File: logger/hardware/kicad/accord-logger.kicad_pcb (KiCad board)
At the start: 2 copper layers, 120 x 80 mm, 72 parts, among them J1 Board connector 14-way, J3 Spare GP13 / switched power, J4 Reset RUN-GND, J5 SD breakout 6-way, Q5 IPD50P04P4L-11, Q6 2N3904, Q7 2N3904, U1 RaspberryPi_Pico_W, U15 MAX3485, U16 DS3231SN, U6 LM2678T-5.0

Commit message: layout: thermal relief fixed at J1 pin 2 and Q6 pin 1
Ground tracks added at both pads. Refilled scratch DRC: no errors beyond
the Pico footprint's own paste items; parity 0; unconnected only Q5's
middle lead; the SUPPLY_ADC via and VSS_IN stub are intentional.

Claude-Session-ID: 42dd0e33-28b5-4936-847e-9c2e1d2488fa
Co-Authored-By: Claude Opus 5.5 <noreply@anthropic.com>
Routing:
- net /PGND: track 40.8 -> 51.8 mm, vias 18 -> 22
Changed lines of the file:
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@@
 		(net 3)
 	)
+	(segment
+		(start 183.515 92.71)
+		(end 184.025 92.2)
+		(width 0.3)
+		(layer "F.Cu")
+		(net 4)
+	)
+	(segment
+		(start 184.025 92.2)
+		(end 185.7325 92.2)
+		(width 0.3)
+		(layer "F.Cu")
+		(net 4)
+	)
+	(segment
+		(start 152.4 101.6)
+		(end 152.4 100.965)
+		(width 0.3)
+		(layer "F.Cu")
+		(net 4)
+	)
+	(segment
+		(start 187.96 92.71)
+		(end 187.45 92.2)
+		(width 0.3)
+		(layer "F.Cu")
+		(net 4)
+	)
+	(segment
+		(start 187.45 92.2)
+		(end 185.7325 92.2)
+		(width 0.3)
+		(layer "F.Cu")
+		(net 4)
+	)
+	(segment
+		(start 152.4 100.965)
+		(end 153.67 99.695)
+		(width 0.3)
+		(layer "F.Cu")
+		(net 4)
+	)
 	(via
 		(at 151.765 79.375)
@@
 	)
 	(via
+		(at 183.515 92.71)
+		(size 0.6)
+		(drill 0.3)
+		(layers "F.Cu" "B.Cu")
+		(net 4)
+	)
+	(via
 		(at 153.035 78.74)
 		(size 0.6)
@@
 	)
 	(via
+		(at 152.4 101.6)
+		(size 0.6)
+		(drill 0.3)
+		(layers "F.Cu" "B.Cu")
+		(net 4)
+	)
+	(via
 		(at 142.875 77.47)
 		(size 0.6)
@@
 	)
 	(via
+		(at 154.94 96.52)
+		(size 0.6)
+		(drill 0.3)
+		(layers "F.Cu" "B.Cu")
+		(net 4)
+	)
+	(via
 		(at 139.7 79.375)
 		(size 0.6)
@@
 	)
 	(via
+		(at 187.96 92.71)
+		(size 0.6)
+		(drill 0.3)
+		(layers "F.Cu" "B.Cu")
+		(net 4)
+	)
+	(via
 		(at 142.875 82.55)
 		(size 0.6)
@@
 		(layers "F.Cu" "B.Cu")
 		(free yes)
+		(net 4)
+	)
+	(segment
+		(start 153.67 97.79)
+		(end 154.94 96.52)
+		(width 0.3)
+		(layer "B.Cu")
 		(net 4)
 	)
@@
 		(layer "B.Cu")
 		(net 4)
+	)
+	(segment
+		(start 153.67 99.695)
+		(end 153.67 97.79)
+		(width 0.3)
+		(layer "B.Cu")
+		(net 4)

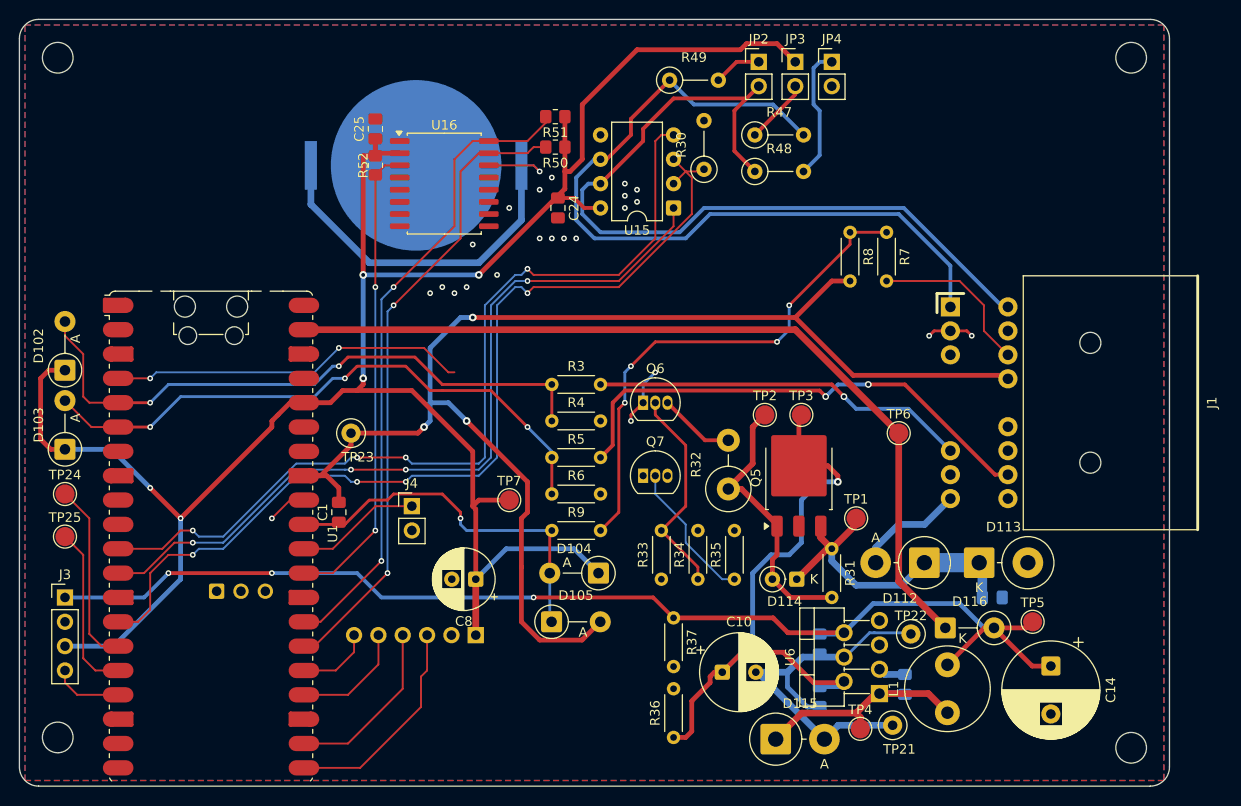
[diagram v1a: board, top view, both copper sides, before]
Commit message: layout: in_supply placed and routed
Owner switched on in_supply (seven on_board flags). After review: GP27
joined to the supply cell; C2, D106 and D107 moved to the pin (8.7-11.4 mm
from U1.32, beside C1); D108 moved toward J1 pin 5 (13.7 mm); the
SUPPLY_ADC via cleared of FUEL_ADC; J4 moved to (141.0, 132.7).
Copper floods: GP27 reaches R12, C2, D106, D107; GP26 reaches R9, C1,
D104, D105; AGND stays one trace off the pour.

Refilled scratch DRC: parity 0, no errors beyond the Pico footprint's own
paste items, unconnected only Q5's middle lead; the VSS_IN stub is
intentional.

Claude-Session-ID: 42dd0e33-28b5-4936-847e-9c2e1d2488fa
Co-Authored-By: Claude Opus 5.5 <noreply@anthropic.com>
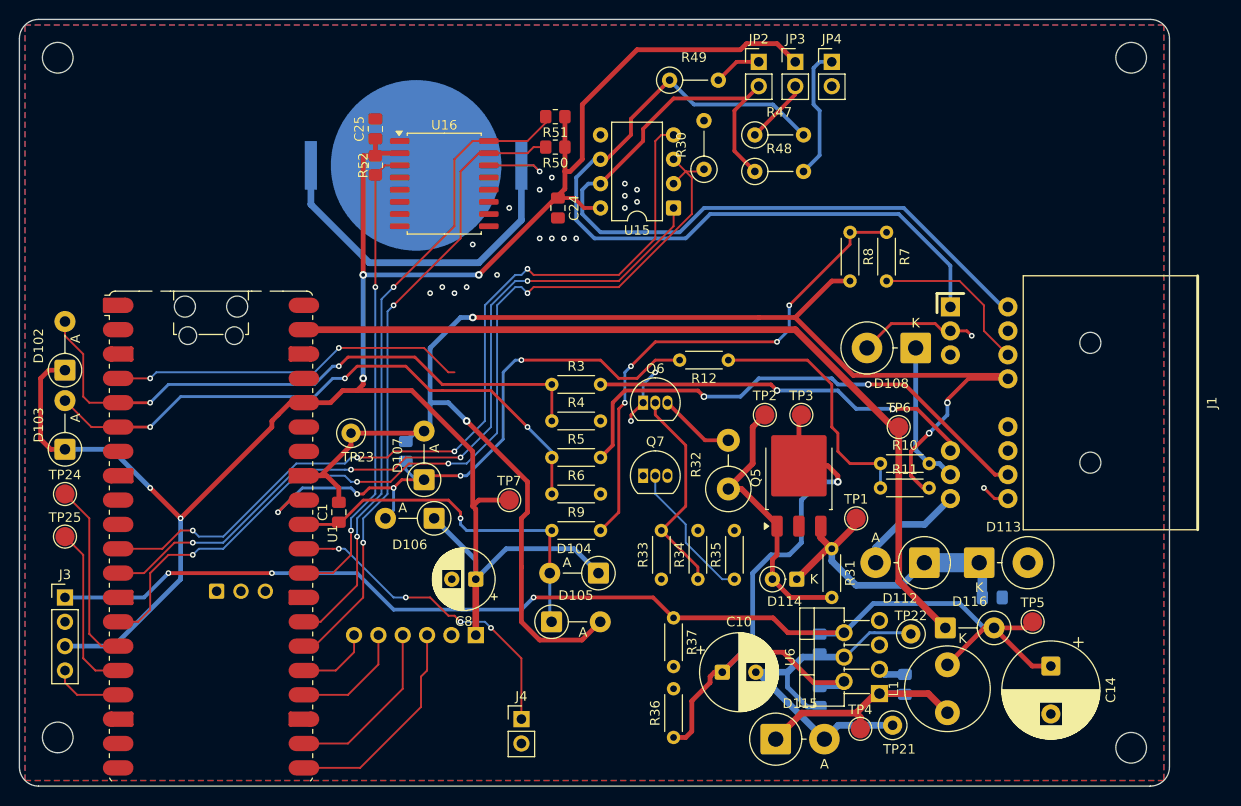
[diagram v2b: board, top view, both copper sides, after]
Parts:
- added C2: 1uF, Capacitor_SMD:C_0805_2012Metric_Pad1.18x1.45mm_HandSolder, B.Cu at (128.9, 104.8)
- added D106: 1N5819, Diode_THT:D_DO-41_SOD81_P5.08mm_Vertical_AnodeUp, F.Cu at (131.9, 111.8)
- added D107: 1N5819, Diode_THT:D_DO-41_SOD81_P5.08mm_Vertical_AnodeUp, F.Cu at (130.8, 107.7)
- added D108: 1.5KE20A-E3/54, Diode_THT:D_DO-201AD_P5.08mm_Vertical_KathodeUp, F.Cu at (182.1, 94.0)
- added R10: 22k, Resistor_THT:R_Axial_DIN0204_L3.6mm_D1.6mm_P5.08mm_Horizontal, F.Cu at (183.5, 106.0)
- added R11: 4.7k, Resistor_THT:R_Axial_DIN0204_L3.6mm_D1.6mm_P5.08mm_Horizontal, F.Cu at (178.4, 108.6)
- added R12: 1k, Resistor_THT:R_Axial_DIN0204_L3.6mm_D1.6mm_P5.08mm_Horizontal, F.Cu at (162.6, 95.2)
- moved J4 25.0 mm to (141.0, 132.7)
- moved TP6 0.64 mm to (180.3, 102.2)
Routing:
- net /SUPPLY_ADC: track 4.13 -> 64.6 mm, vias 1 -> 5
- net /SUPPLY_DIV: track 0.00 -> 26.6 mm
- net /AGND: track 139.4 -> 161.1 mm, vias 3 -> 4
- net /RUN: track 13.1 -> 33.8 mm, vias 0 -> 4
- net /B11_TAP: track 0.00 -> 15.5 mm
- net /PGND: track 51.8 -> 62.4 mm
- net /P3V3_SW: track 227.8 -> 235.9 mm
- net /UART1_TX: track 92.7 -> 89.9 mm
- net /UART1_RX: track 84.2 -> 82.3 mm
- net /BUS_DE: track 100.4 -> 98.9 mm
- net /B5: track 123.8 -> 124.9 mm
- net /FUEL_ADC: track 39.2 -> 38.7 mm
- net /C14_TAP: track 52.7 -> 53.2 mm
- net /B1_TAP: track 39.4 -> 39.9 mm, vias 1 -> 2

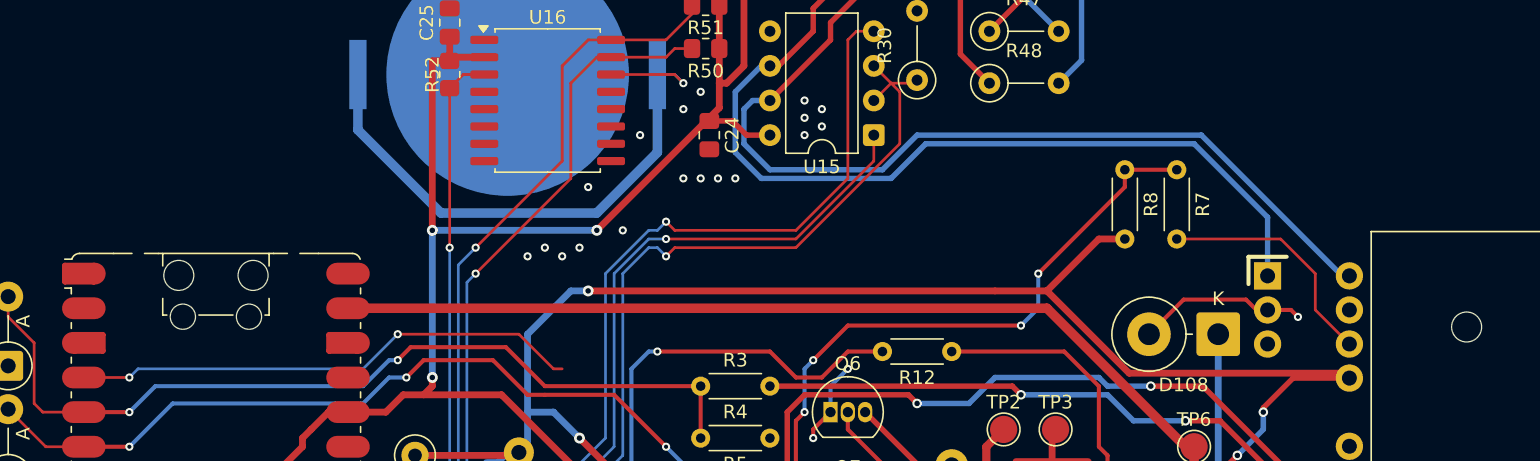
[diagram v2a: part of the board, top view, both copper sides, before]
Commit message: layout: in_vss placed and routed
Owner switched on in_vss (U3, R1, R2, D101; four on_board flags). U3
ASSR-601JV on the back by J1. Copper floods: J1.3 (B2) reaches U3 pins
15/16; B2_ISO joins U3 pins 9 and 10 to R1; VSS_IN reaches R1, R2, D101
and GP2. After review: U3 pin 9 tied to pin 10, the RS485_B via cleared
of VSS_IN, J1 pin 2 thermal relief fixed again. U3's LED pins wait for
iso_enable.

Refilled scratch DRC: parity 0, no errors beyond the Pico footprint's own
paste items, unconnected only Q5's middle lead.

Claude-Session-ID: 42dd0e33-28b5-4936-847e-9c2e1d2488fa
Co-Authored-By: Claude Opus 5.5 <noreply@anthropic.com>
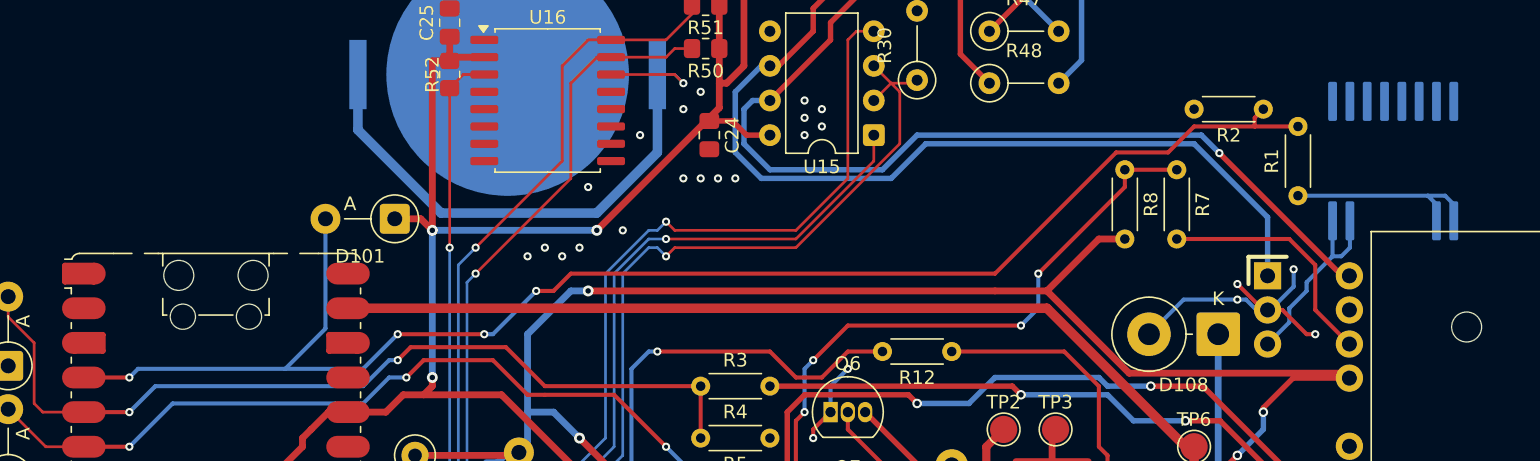
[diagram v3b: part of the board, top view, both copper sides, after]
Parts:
- added D101: 1N5819, Diode_THT:D_DO-41_SOD81_P5.08mm_Vertical_AnodeUp, F.Cu at (121.7, 85.5)
- added R1: 22k, Resistor_THT:R_Axial_DIN0204_L3.6mm_D1.6mm_P5.08mm_Horizontal, F.Cu at (188.0, 83.8)
- added R2: 33k, Resistor_THT:R_Axial_DIN0204_L3.6mm_D1.6mm_P5.08mm_Horizontal, F.Cu at (185.4, 77.5)
- added U3: ASSR-601JV, accord-logger:ASSR-601Jx_SO-16-12Lead_11.634x10.363mm_P1.27mm, B.Cu at (194.9, 81.3)
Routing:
- net /VSS_IN: track 37.5 -> 110.5 mm, vias 2 -> 4
- net /B2_ISO: track 0.00 -> 15.0 mm
- net /B2_TAP: track 0.00 -> 14.5 mm
- net /PGND: track 62.4 -> 71.1 mm, vias 22 -> 25
- net /P3V3_SW: track 235.9 -> 239.0 mm
- net /RS485_B: vias 0 -> 1

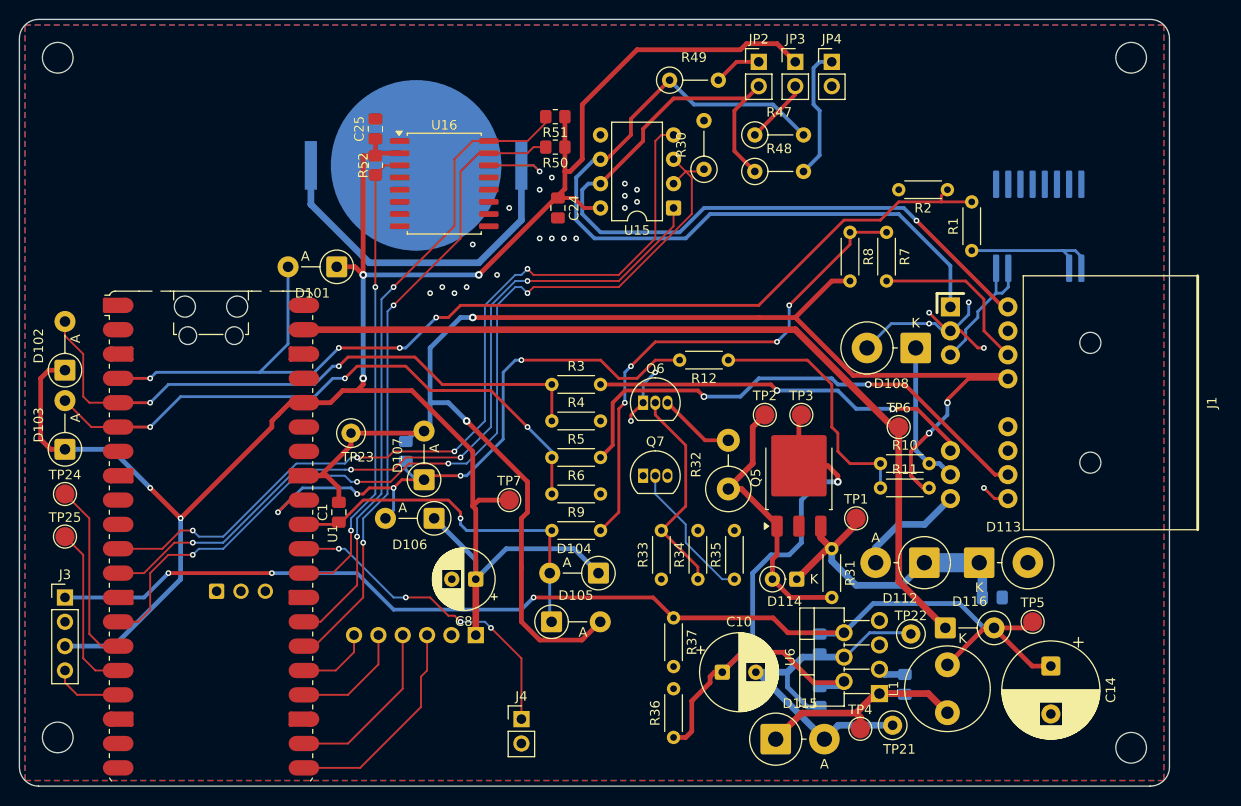
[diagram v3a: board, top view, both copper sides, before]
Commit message: layout: ign_opto placed and routed
Owner switched on ign_opto (D109, R13, D110, U2; four on_board flags).
D109 by J1 on B11_TAP; R13 (DIN0414 vertical) and U2 PC817 to its left;
D110 1N4148W on the back across the LED. IGN_POS runs D109 -> R13 and on
to R33 pin 1 (QI base), 0.4 mm, three vias. U2 pins 3/4 (IGN_A, A5) wait
for qual_rc and a5_reg.

Refilled scratch DRC: parity 0, no errors beyond the Pico footprint's own
paste items, unconnected only Q5's middle lead. ERC 0; full-netlist
capture 782/782; closure 67/67.

Claude-Session-ID: d2c32eb9-406b-48d8-b5b5-bb1d8d4746af
Co-Authored-By: Claude Opus 5.5 <noreply@anthropic.com>
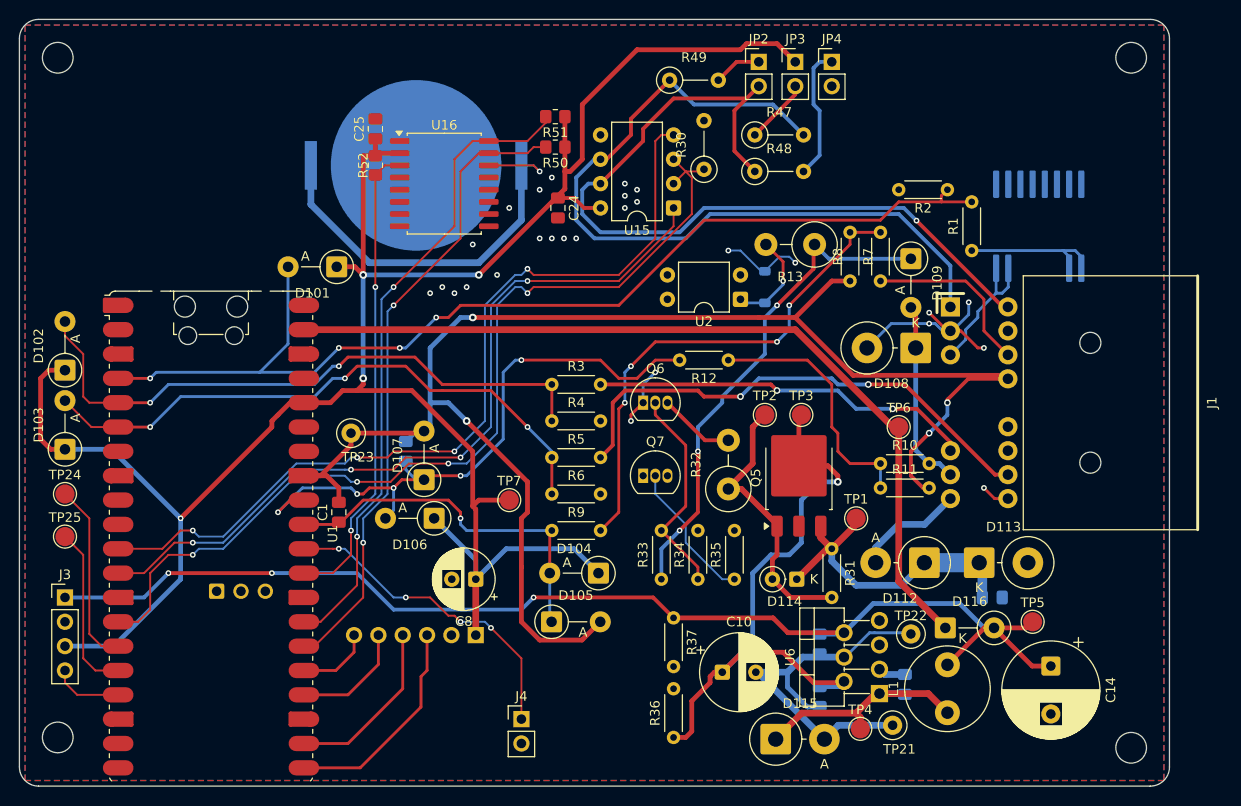
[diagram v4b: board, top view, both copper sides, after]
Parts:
- added D109: 1N5819, Diode_THT:D_DO-41_SOD81_P5.08mm_Vertical_AnodeUp, F.Cu at (181.6, 84.7)
- added D110: 1N4148W, Diode_SMD:D_SOD-123, B.Cu at (166.4, 87.6)
- added R13: 2.2k, Resistor_THT:R_Axial_DIN0414_L11.9mm_D4.5mm_P5.08mm_Vertical, F.Cu at (171.6, 83.2)
- added U2: PC817, Package_DIP:DIP-4_W7.62mm, F.Cu at (163.8, 88.9)
- moved R7 0.63 mm to (178.4, 87.0)
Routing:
- net /IGN_POS: track 0.00 -> 52.2 mm, vias 0 -> 3
- net /IGN_LED_A: track 0.00 -> 11.2 mm, vias 0 -> 1
- net /PGND: track 71.1 -> 79.9 mm, vias 25 -> 27
- net /B11_TAP: track 15.5 -> 20.0 mm
- net /FUEL_DIV: track 53.1 -> 52.5 mm
- net /P3V3_SW: vias 5 -> 4
